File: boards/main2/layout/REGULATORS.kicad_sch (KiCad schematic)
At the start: 28 parts, among them IC7 L6981C33DR, J1 B02B-PASK(LF)(SN), Q6 HSBB3072, Q8 AO3401A, SW4 SK-12D29-G060, U8 ADP7142ACPZN3.3-R7

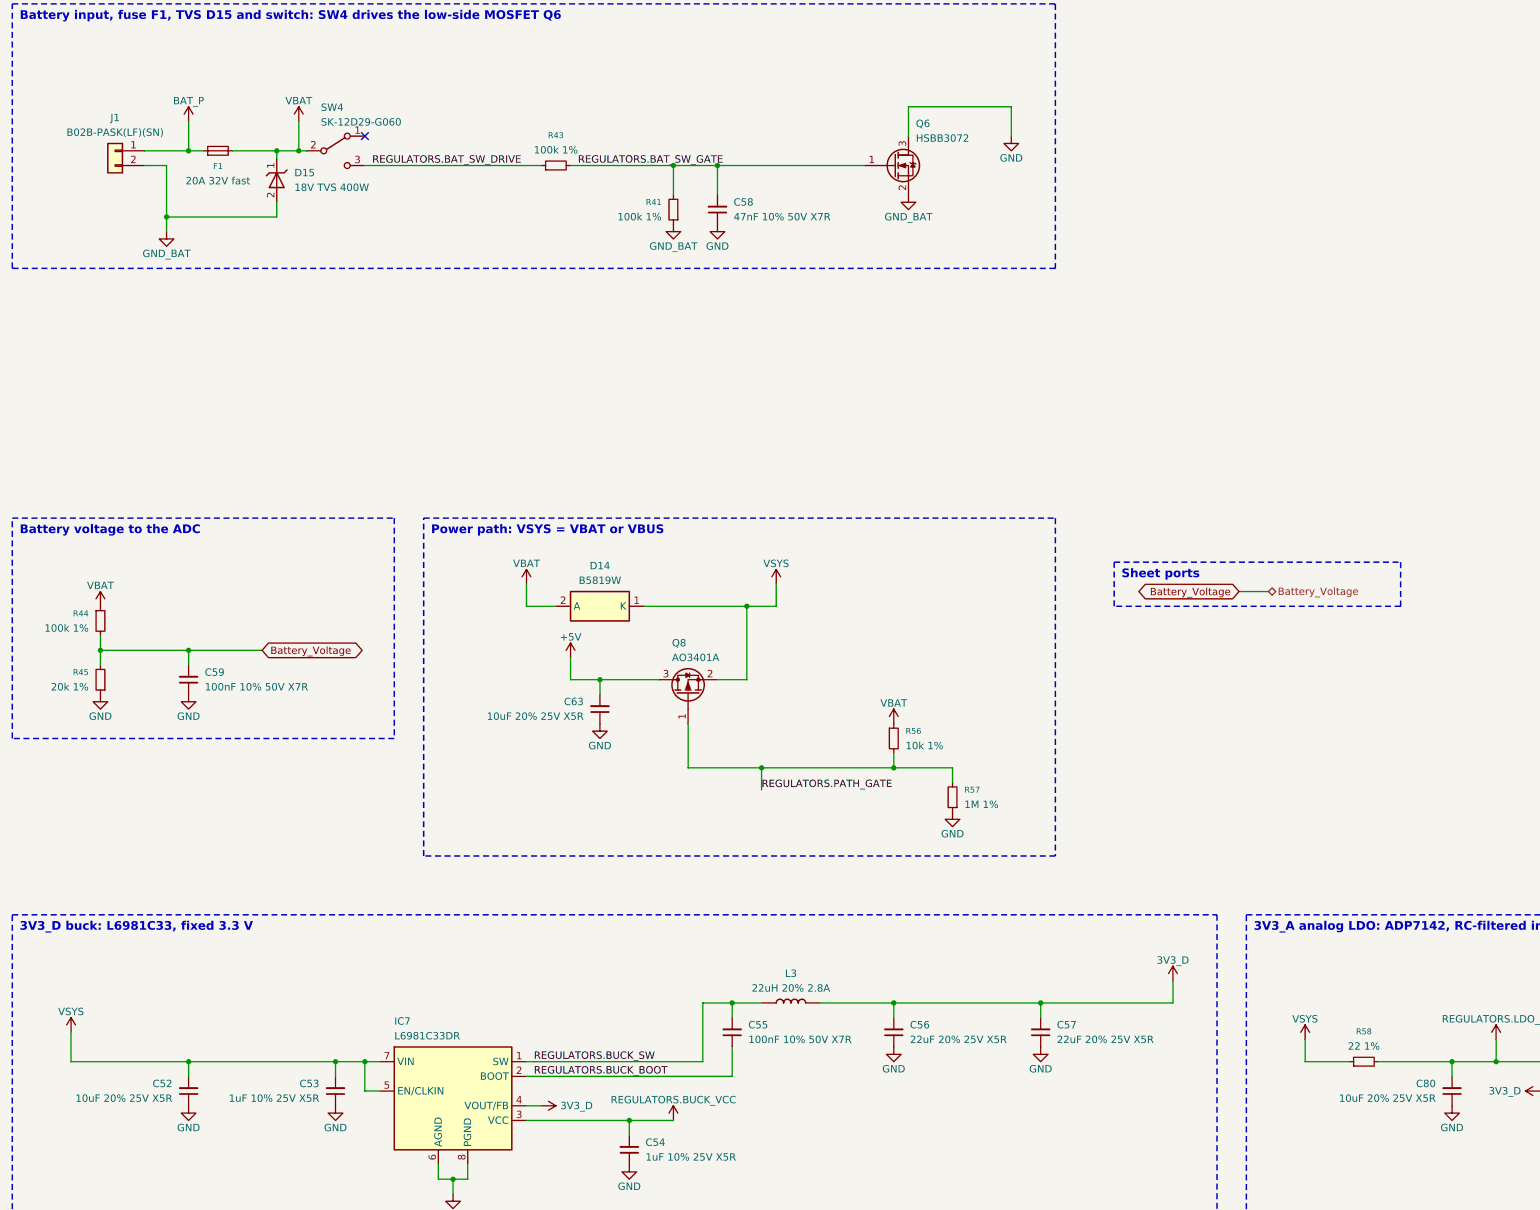
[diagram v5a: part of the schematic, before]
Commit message: 🐛 Fix main2's review findings and settle its open doubts
Schematic and parts:
- Battery input: F1 is a 12 A Littelfuse 501 (0501012.WR1). C58 now sits
  gate-source with C114 gate-drain, so Q6 stays off at plug-in. D16 clamps
  Q8's VGS. R44/R45 are 10k/2k, so VBAT can't float up on USB alone.
- Capacitors: VBAT and VSYS use 1210/0805 50 V parts, sized with Samsung's
  DC-bias curves. C109 is fitted.
- Drivers: R66/R76 are removed (the chokes are needed). ITRIP and the fan
  limit are retuned. The INA241 R_iso is 150 Ohm.
- Rails are declared as ranges, and the abs-max checks run under the TVS
  clamp.
- STM32 pin swaps for routing: the wall selectors move to TIM3,
  Motor_Left_EN to TIM8_CH2 and LED_ARGB to TIM17. CubeMX 6.18.1 confirms
  the map.
- firmware_changes.toml registers the matching firmware changes: the ADC
  0.7 us sampling time, the TIM4-triggered DAC, the fan's 50 kHz start, a
  wheel-sign self-check, VDDA tracking, contest mode, the debug halt and
  others.

Layout:
- USB D+/D- are routed as a coupled pair. The track floor is 0.12 mm.
- Stubs and detours are trimmed. The In2 VCORE/3V3_D islands are shrunk.
- The board is notched under the ESP32 antenna.
- Ground stitching, thermal reliefs, open thermal vias with split paste,
  DRV8874 heat islands and teardrops are added.
- 11 joins remain for hand-routing (layout README, Open items).

Doubts are closed by datasheets, vendor SPICE models and new research
calculations instead of bench TODOs. Tests cover each review item.
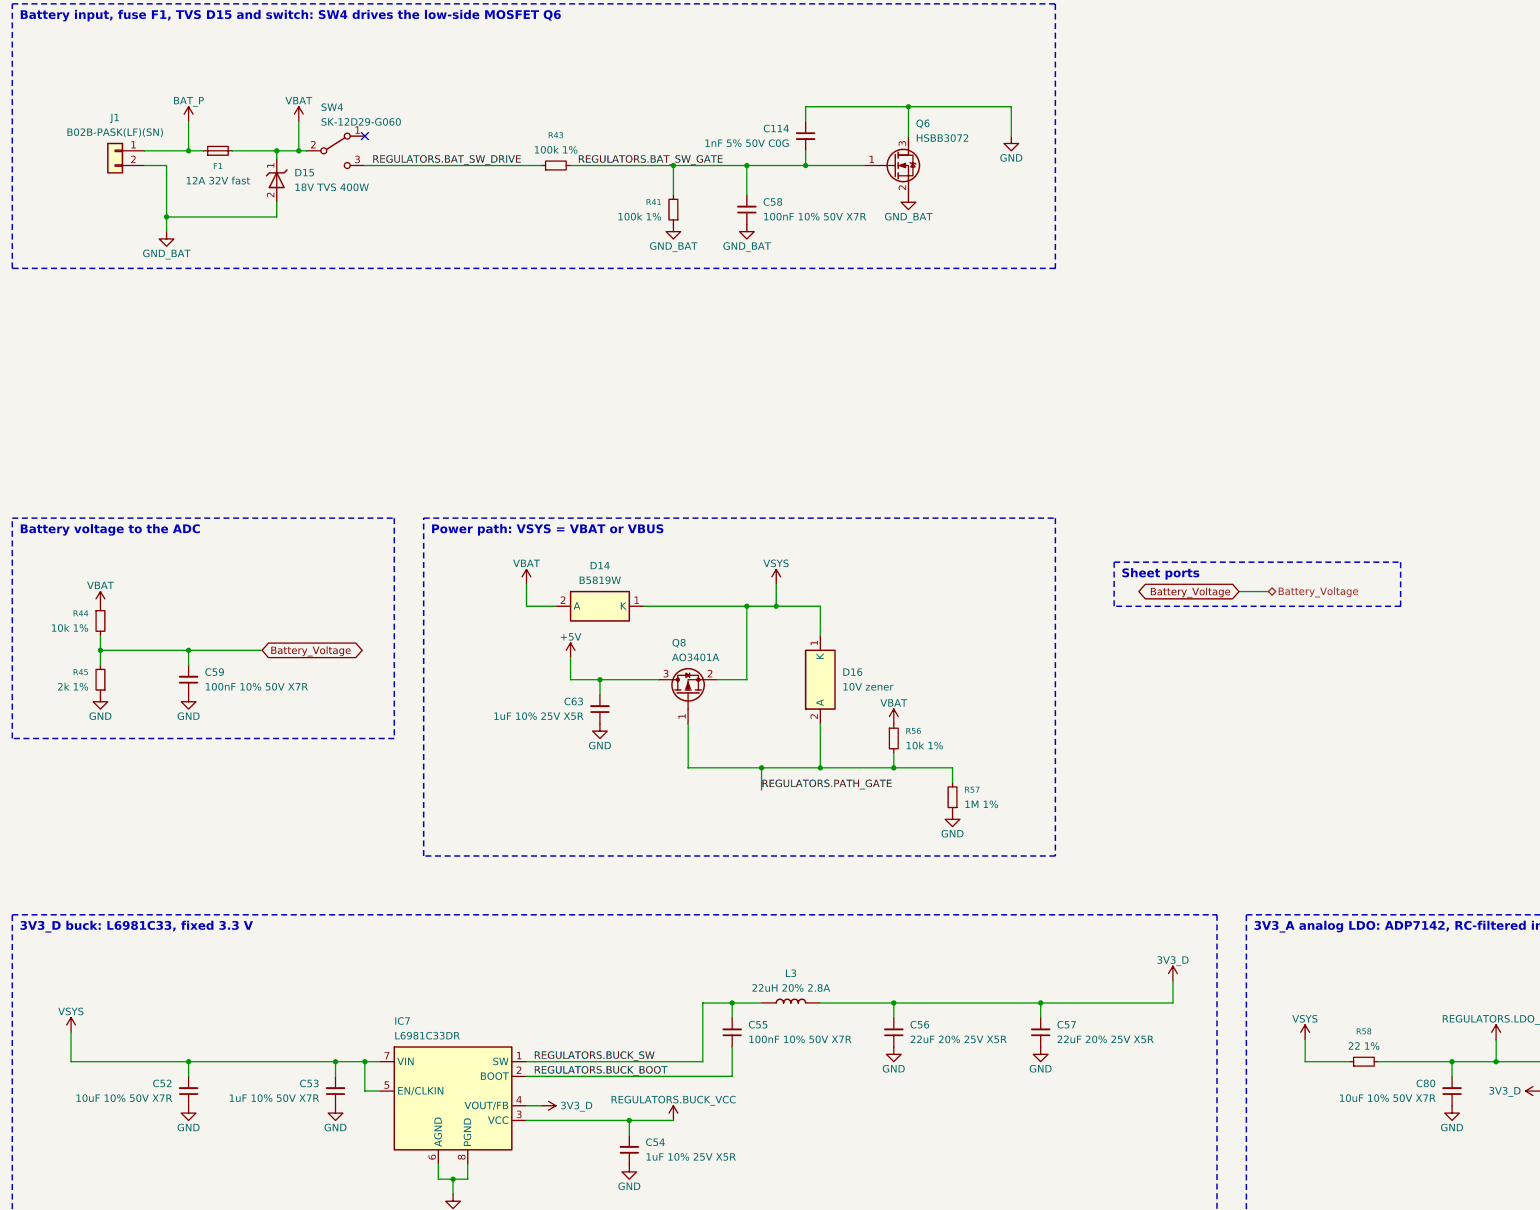
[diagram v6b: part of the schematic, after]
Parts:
- added C114: 1nF 5% 50V C0G, stdlib_kicad-footprints_Capacitor_SMD:C_0402_1005Metric, symbol C_Small
- added D16: 10V zener, Team-Micras_MicrasPCB_components_diodes_BZT52C10S:D_SOD-323, symbol BZT52C10S-7-F
- C52, C80: value 10uF 20% 25V X5R -> 10uF 10% 50V X7R; footprint stdlib_kicad-footprints_Capacitor_SMD:C_0603_1608Metric -> stdlib_kicad-footprints_Capacitor_SMD:C_1210_3225Metric
- C53: value 1uF 10% 25V X5R -> 1uF 10% 50V X7R; footprint stdlib_kicad-footprints_Capacitor_SMD:C_0402_1005Metric -> stdlib_kicad-footprints_Capacitor_SMD:C_0805_2012Metric
- C58: value 47nF 10% 50V X7R -> 100nF 10% 50V X7R; footprint stdlib_kicad-footprints_Capacitor_SMD:C_0603_1608Metric -> stdlib_kicad-footprints_Capacitor_SMD:C_0402_1005Metric
- C63: value 10uF 20% 25V X5R -> 1uF 10% 25V X5R; footprint stdlib_kicad-footprints_Capacitor_SMD:C_0603_1608Metric -> stdlib_kicad-footprints_Capacitor_SMD:C_0402_1005Metric
- F1: value 20A 32V fast -> 12A 32V fast; footprint Team-Micras_MicrasPCB_components_littelfuse_0501020:Fuse_Littelfuse_501_1206 -> Team-Micras_MicrasPCB_components_littelfuse_05010xx:Fuse_Littelfuse_501_1206; symbol 0501020 -> 05010xx
- Q6: footprint Team-Micras_MicrasPCB_components_huashuo_HSBB3072:PRPAK-8_L3.0-W3.0-P0.65-BL-EP -> Team-Micras_MicrasPCB_components_huashuo_HSBB3072:PRPAK-8_L3.0-W3.0-P0.65-BL-EP_SplitPaste
- R44: value 100k 1% -> 10k 1%
- R45: value 20k 1% -> 2k 1%
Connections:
- net GND: now also C114.1; no longer C58.1
- net GND_BAT: now also C58.1
- net REGULATORS.BAT_SW_GATE: now also C114.2
- net REGULATORS.PATH_GATE: now also D16.2 (A)
- net VSYS: now also D16.1 (K)
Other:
- moved on the sheet: C58
